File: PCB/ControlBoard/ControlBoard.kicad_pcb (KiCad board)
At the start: 4 copper layers, 98 x 58 mm, 101 parts, among them J1 SWD, J10 BUSPWR, J11 BATT +, J12 BATT -, J2 USB, J3 Bus, J4 Submodule A, J5 Submodule B, J6 Submodule C, J7 uSD, J8 ARGB, J9 Indicator, SW1 Boot, U1 STM32H562VGT6, U2 MCP2562-E-SN, U3 TPD2E2U06DCK, U4 SN74AHCT1G125, U5 TPS629210, U6 TPS629210, U7 CM1293A‐04SO, U8 TPS22918, Y1 XO22C3EREHX50M000, Y2 32.768k

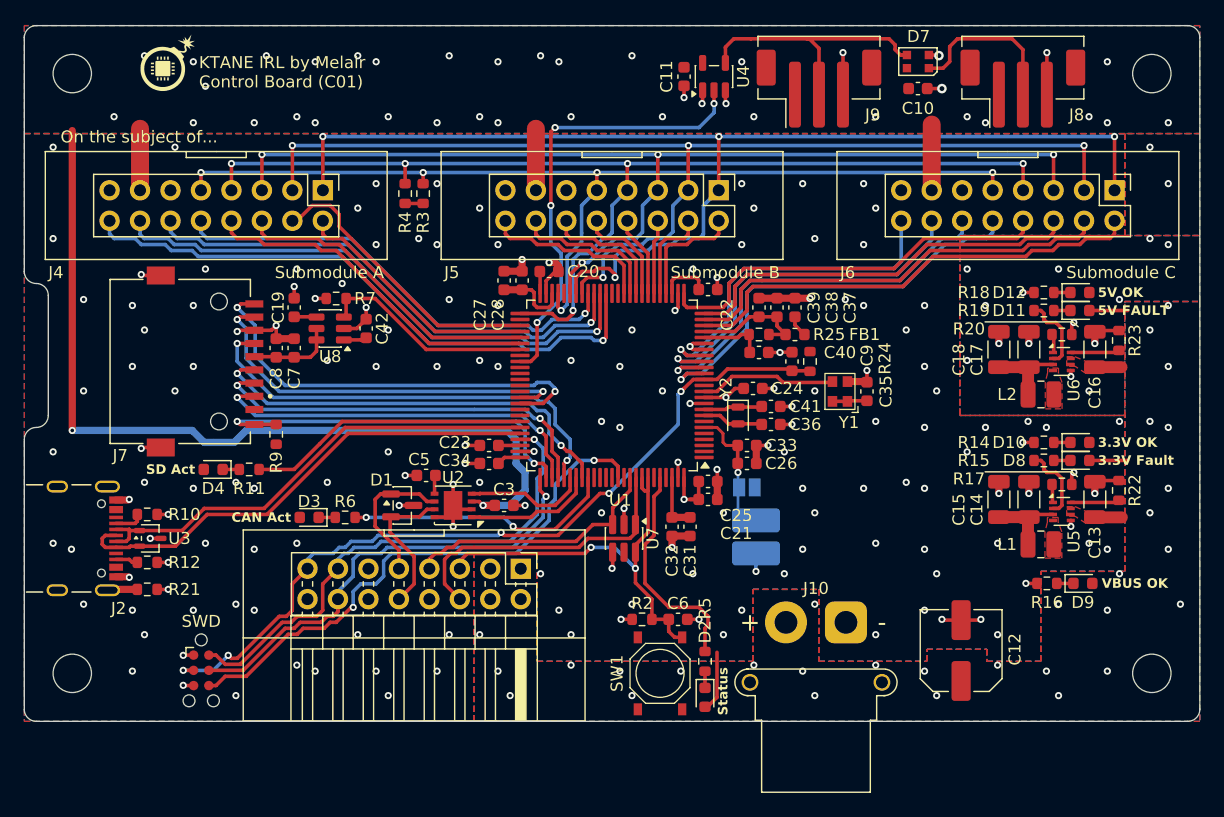
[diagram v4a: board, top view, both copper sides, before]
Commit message: feat: Remove backup battery for RTC, and crystal. 1PPS can be derived from HSE.
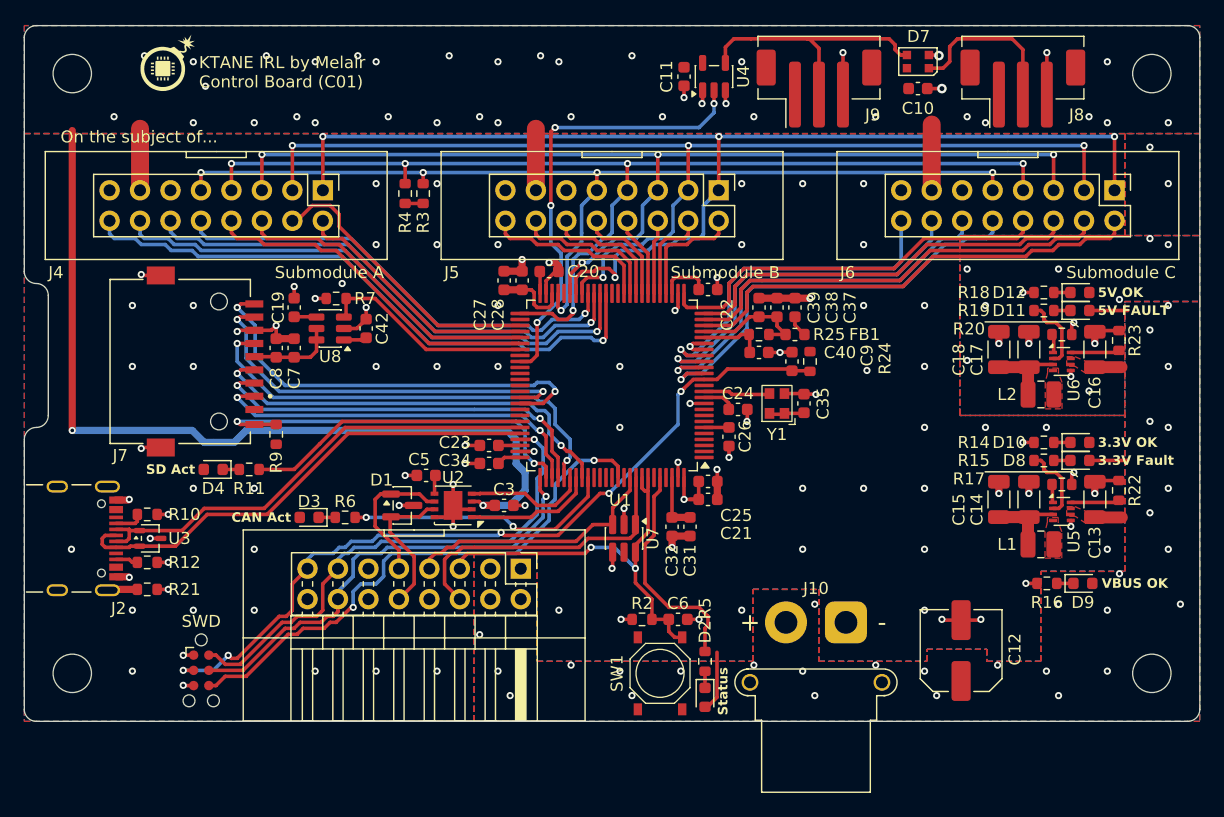
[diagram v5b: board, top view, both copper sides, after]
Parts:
- removed C33: 1μF, Capacitor_SMD:C_0603_1608Metric
- removed C36, C41: 8pF, Capacitor_SMD:C_0603_1608Metric
- removed J11: BATT +, KTANE:Pad4x2
- removed J12: BATT -, KTANE:Pad4x2
- removed JP1: NoBatt, Jumper:SolderJumper-2_P1.3mm_Open_Pad1.0x1.5mm
- removed Y2: 32.768k, Crystal:Crystal_SMD_2012-2Pin_2.0x1.2mm
- moved C35 5.34 mm to (86.0, 52.5)
- moved Y1 5.34 mm to (83.8, 52.5)
- moved C26 2.68 mm to (79.8, 55.3), turned to -90 degrees
- moved C24 2.15 mm to (80.5, 53.0)
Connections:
- C26 pad 1: +BATT -> +3.3V
- U1 pad 6: +BATT -> +3.3V
- U1 pad 8: Net-(U1-PC14) -> unconnected-(U1-PC14-Pad8)
- U1 pad 9: Net-(U1-PC15) -> unconnected-(U1-PC15-Pad9)
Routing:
- net +BATT: track 10.1 -> 0.00 mm, vias 1 -> 0
- net Net-(U1-PH0): track 11.5 -> 5.58 mm
- net Net-(U1-PC14): track 5.11 -> 0.00 mm
- net GND: track 106.6 -> 101.7 mm, vias 142 -> 140
- net Net-(U1-PC15): track 4.90 -> 0.00 mm
- net +3.3V: track 41.6 -> 42.8 mm, vias 70 -> 3

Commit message: fix: Correct stitching for 3.3V and GND layers.
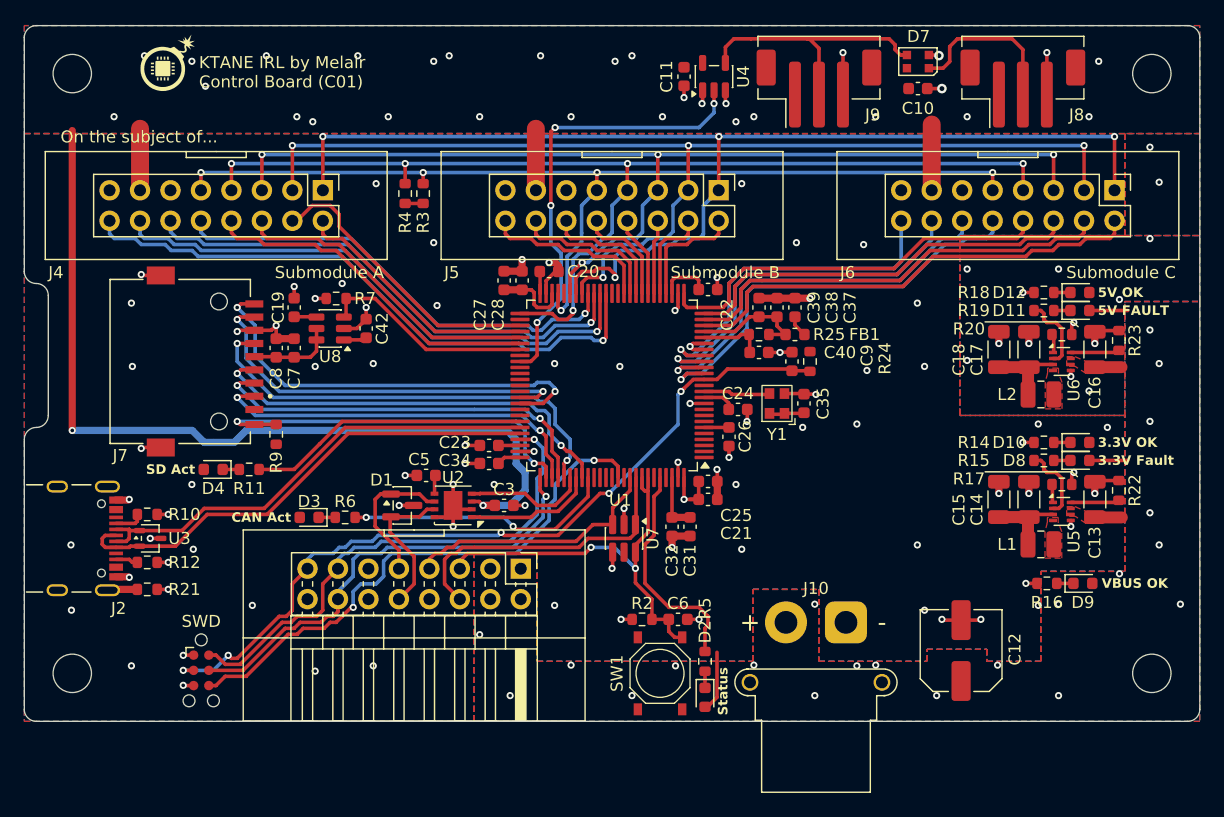
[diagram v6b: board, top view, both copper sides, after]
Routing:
- net GND: vias 140 -> 92
- net +3.3V: vias 3 -> 18
